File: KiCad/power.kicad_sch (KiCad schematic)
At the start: 37 parts, among them J1 JST_PH_2.0mm_1x02, Q1 DMG2305UX-13, Q2 FS8205A, Q3 DMG2305UX-13, Q4 AO3400A, Q5 AO3400A, U1 DW01A, U2 LP5907MFX-3.3/NOPB, U3 TP4056, U4 LP5907MFX-3.3/NOPB, U5 SD6210A

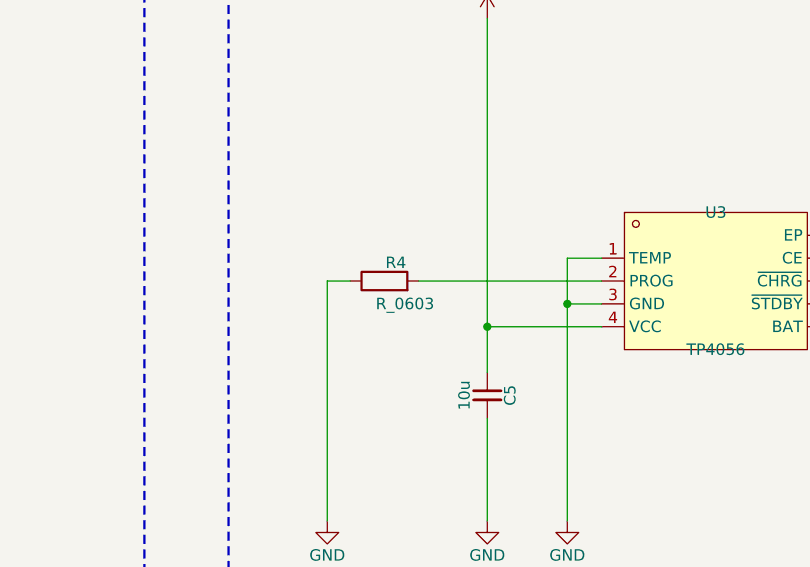
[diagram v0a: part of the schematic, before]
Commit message: R4 changed to 2k
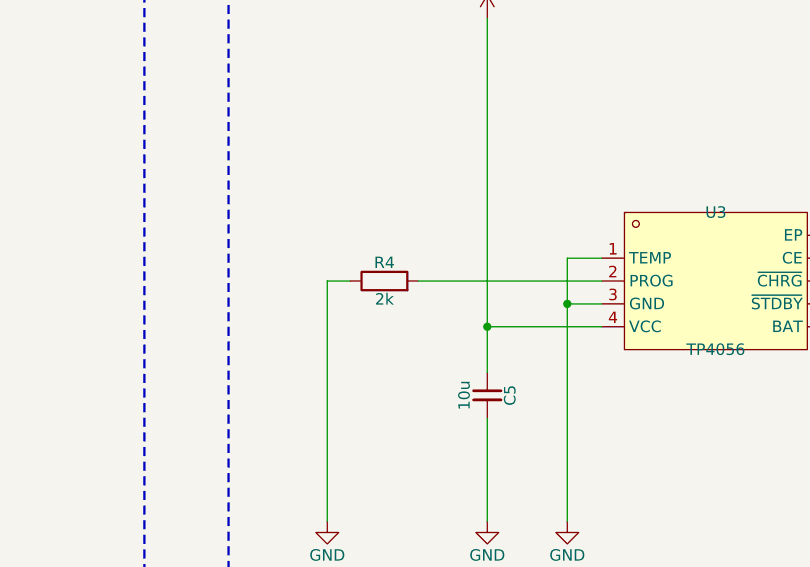
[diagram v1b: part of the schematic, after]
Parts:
- R4: value R_0603 -> 2k; symbol sldrnrd:Resistor/R_0603 -> sldrnrd:Resistor/R0603_2k; LCSC (none) -> C22975; MPN (none) -> 0603WAF2001T5E; Manufacturer (none) -> Uni-Royal
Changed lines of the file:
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@@
 	)
 	(symbol
-		(lib_id "sldrnrd:Resistor/R_0603")
+		(lib_id "sldrnrd:Resistor/R0603_2k")
 		(at 313.69 80.01 90)
 		(unit 1)
@@
 		(dnp no)
 		(property "Reference" "R4"
-			(at 314.96 77.978 90)
+			(at 313.69 77.978 90)
 			(show_name no)
 			(do_not_autoplace no)
@@
 			)
 		)
-		(property "Value" "R_0603"
-			(at 315.976 82.55 90)
+		(property "Value" "2k"
+			(at 313.69 82.042 90)
 			(show_name no)
 			(do_not_autoplace no)
@@
 			)
 		)
-		(property "Description" "Resistor"
+		(property "Description" "2k Resistor, 0603, 1%, 75V, 100mW"
 			(at 313.69 80.01 0)
 			(hide yes)
+			(show_name no)
+			(do_not_autoplace no)
+			(effects
+				(font
+					(size 1.27 1.27)
+				)
+			)
+		)
+		(property "Manufacturer" "Uni-Royal"
+			(at 313.69 80.01 0)
+			(hide yes)
+			(show_name no)
+			(do_not_autoplace no)
+			(effects
+				(font
+					(size 1.27 1.27)
+				)
+			)
+		)
+		(property "MPN" "0603WAF2001T5E"
+			(at 313.69 80.01 0)
+			(hide yes)
+			(show_name no)
+			(do_not_autoplace no)
+			(effects
+				(font
+					(size 1.27 1.27)
+				)
+			)
+		)
+		(property "LCSC" "C22975"
+			(at 313.69 80.01 0)
+			(hide yes)
